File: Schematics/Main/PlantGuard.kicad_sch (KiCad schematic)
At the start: 7 parts, among them M1 Motor_DC, SW1 SW_SP3T, U1 L298N, U2 LM78M05_TO252

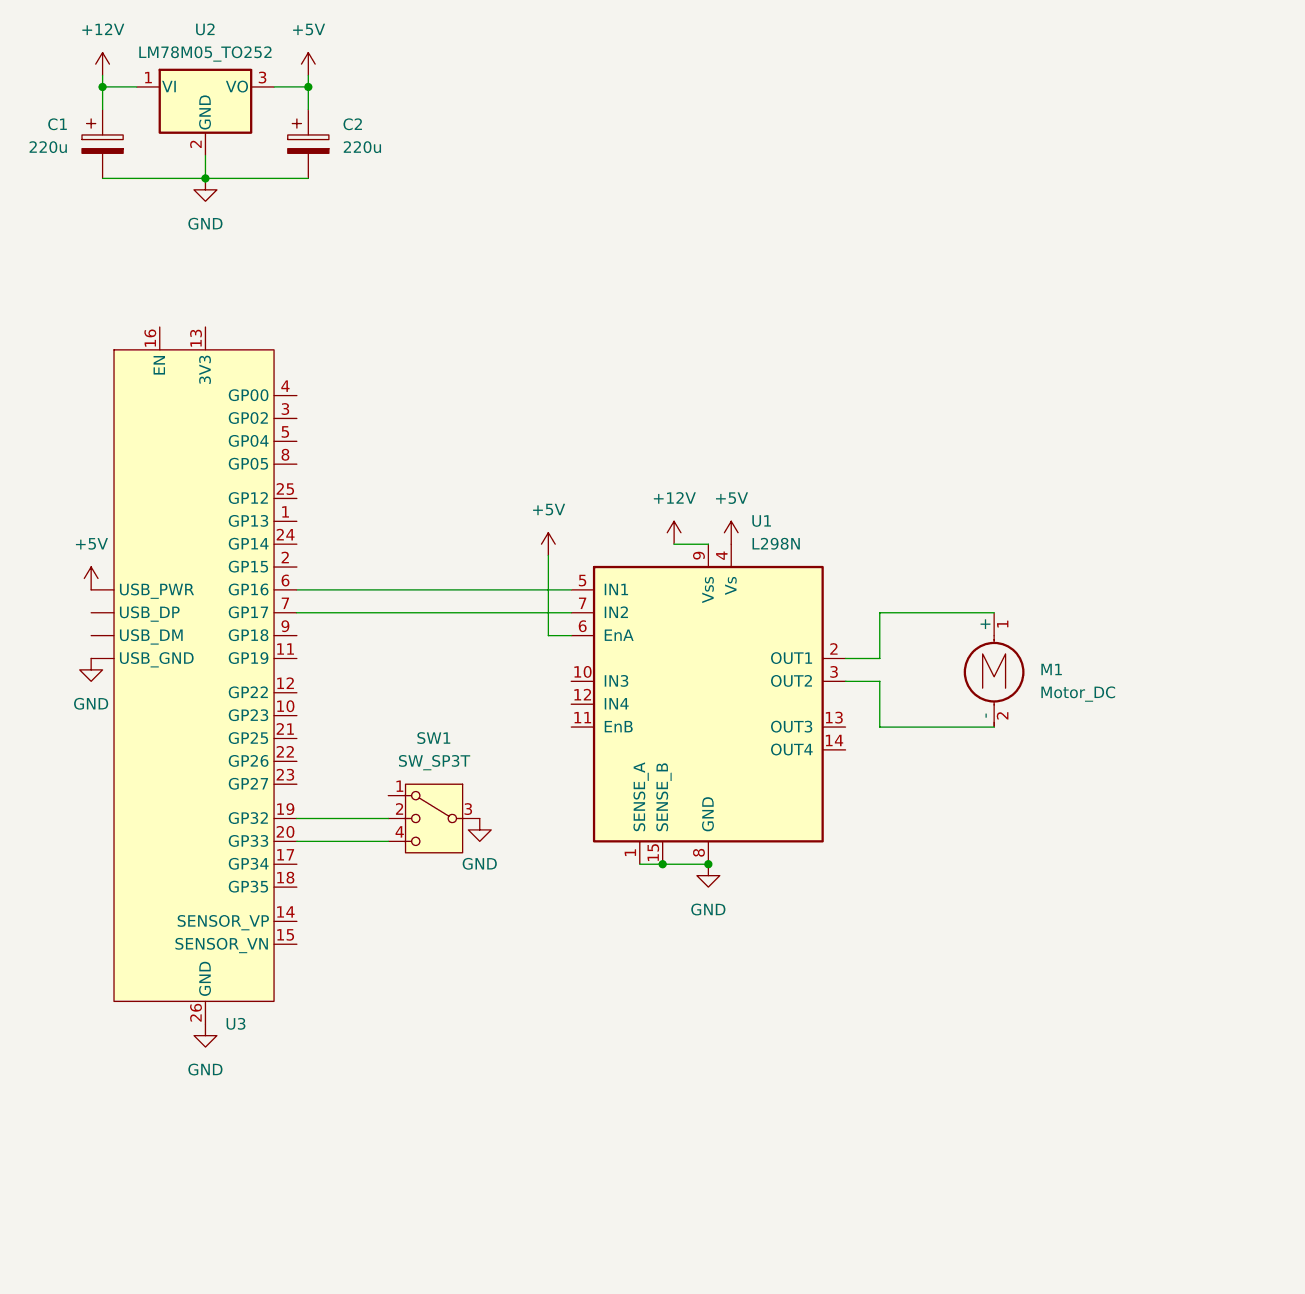
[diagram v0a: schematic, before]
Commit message: Read light intensity from photoresistor
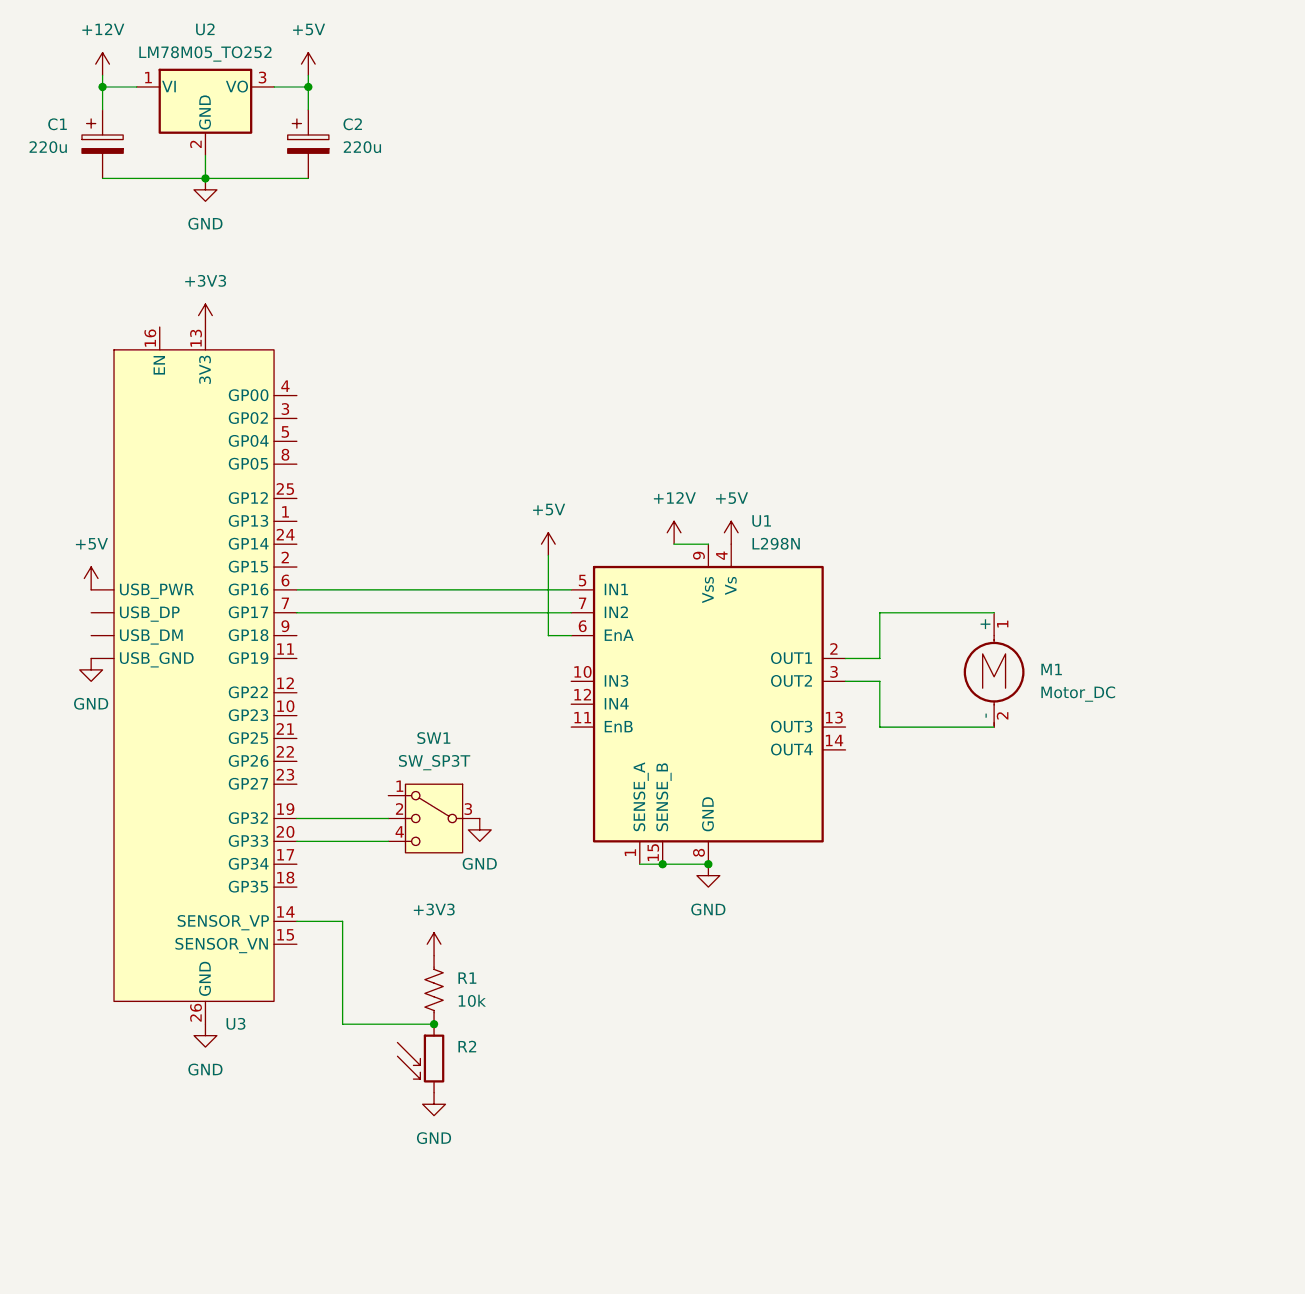
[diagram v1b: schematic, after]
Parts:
- added R1: 10k, symbol Device:R_US
- added R2: (no value), symbol Device:R_Photo
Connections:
- net GND: now also R2.2
- net +3V3: now reaches U3.13 (3V3)
- net +3V3: now also R1.1
- net at U3.14 (SENSOR_VP): now also R1.2, R2.1

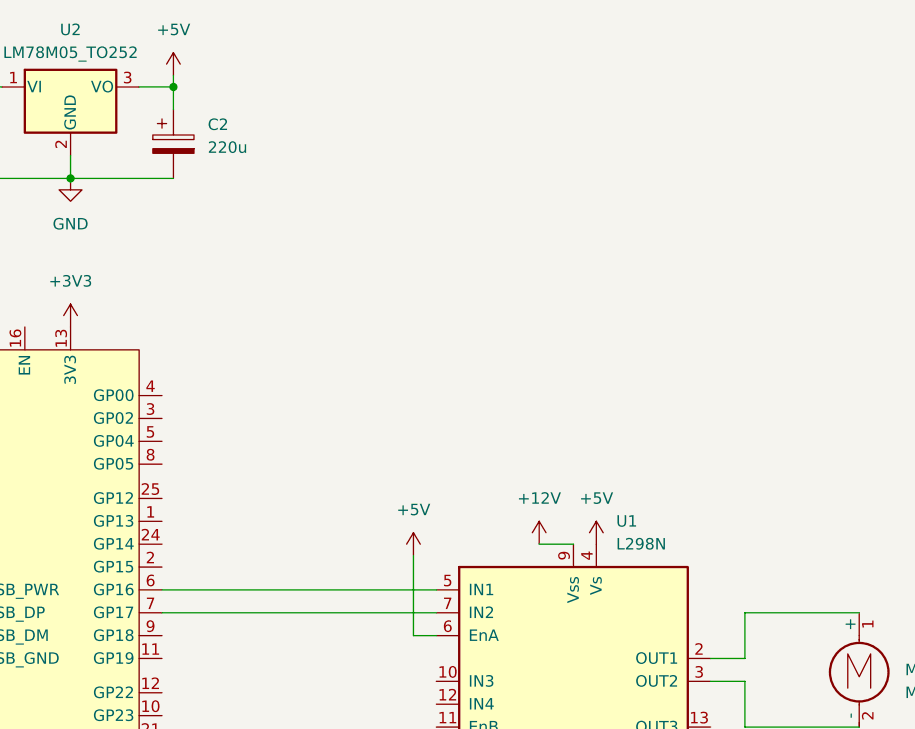
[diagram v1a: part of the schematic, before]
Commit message: Connect the accelerometer
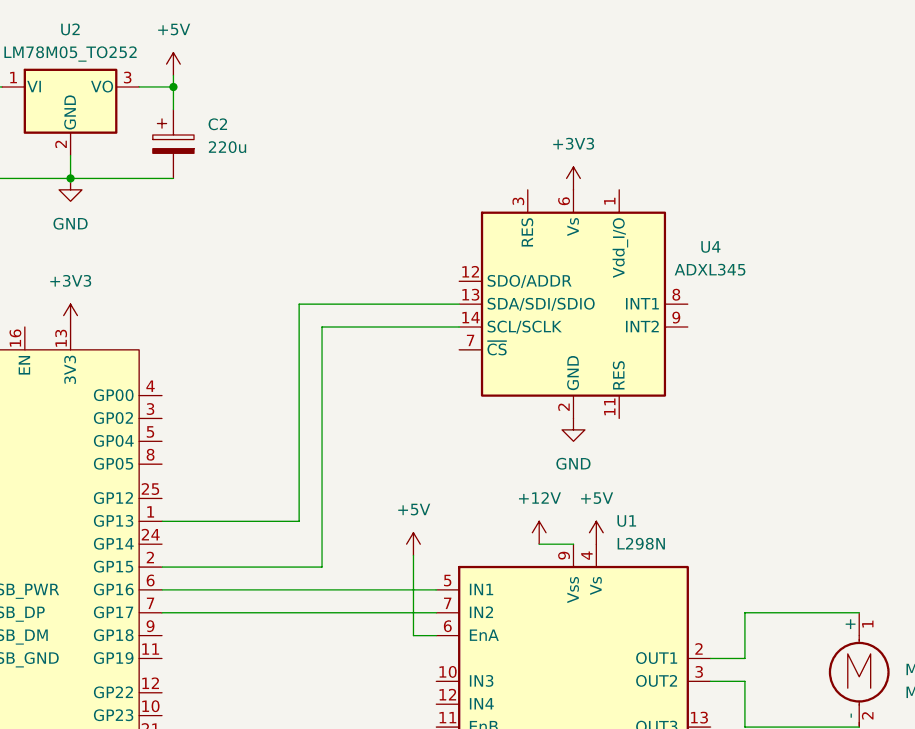
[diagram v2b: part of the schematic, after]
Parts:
- added U4: ADXL345, Package_LGA:LGA-14_3x5mm_P0.8mm_LayoutBorder1x6y, symbol Sensor_Motion:ADXL343
- R2: value (none) -> ~
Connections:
- net +3V3: now also U4.6 (Vs)
- net GND: now also U4.2 (GND), U4.4 (GND), U4.5 (GND)
- net at U3.1 (GP13): now also U4.13 (SDA/SDI/SDIO)
- net at U3.2 (GP15): now also U4.14 (SCL/SCLK)

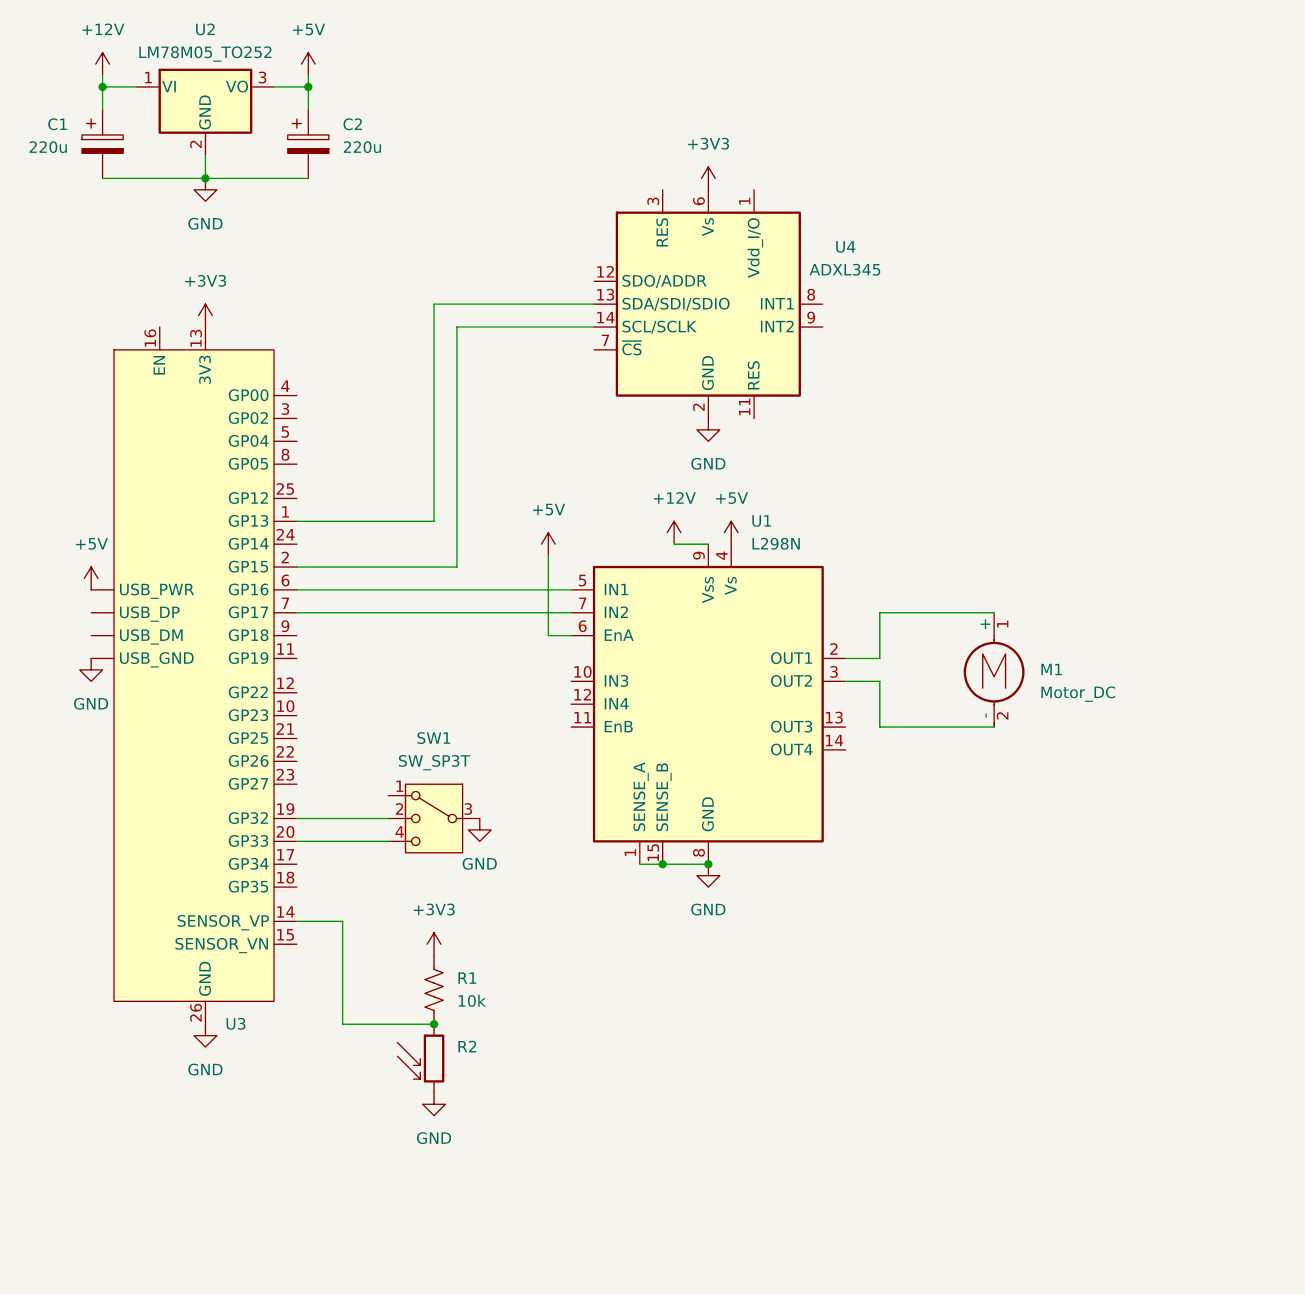
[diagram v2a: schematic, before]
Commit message: Connect ground moisture sensor
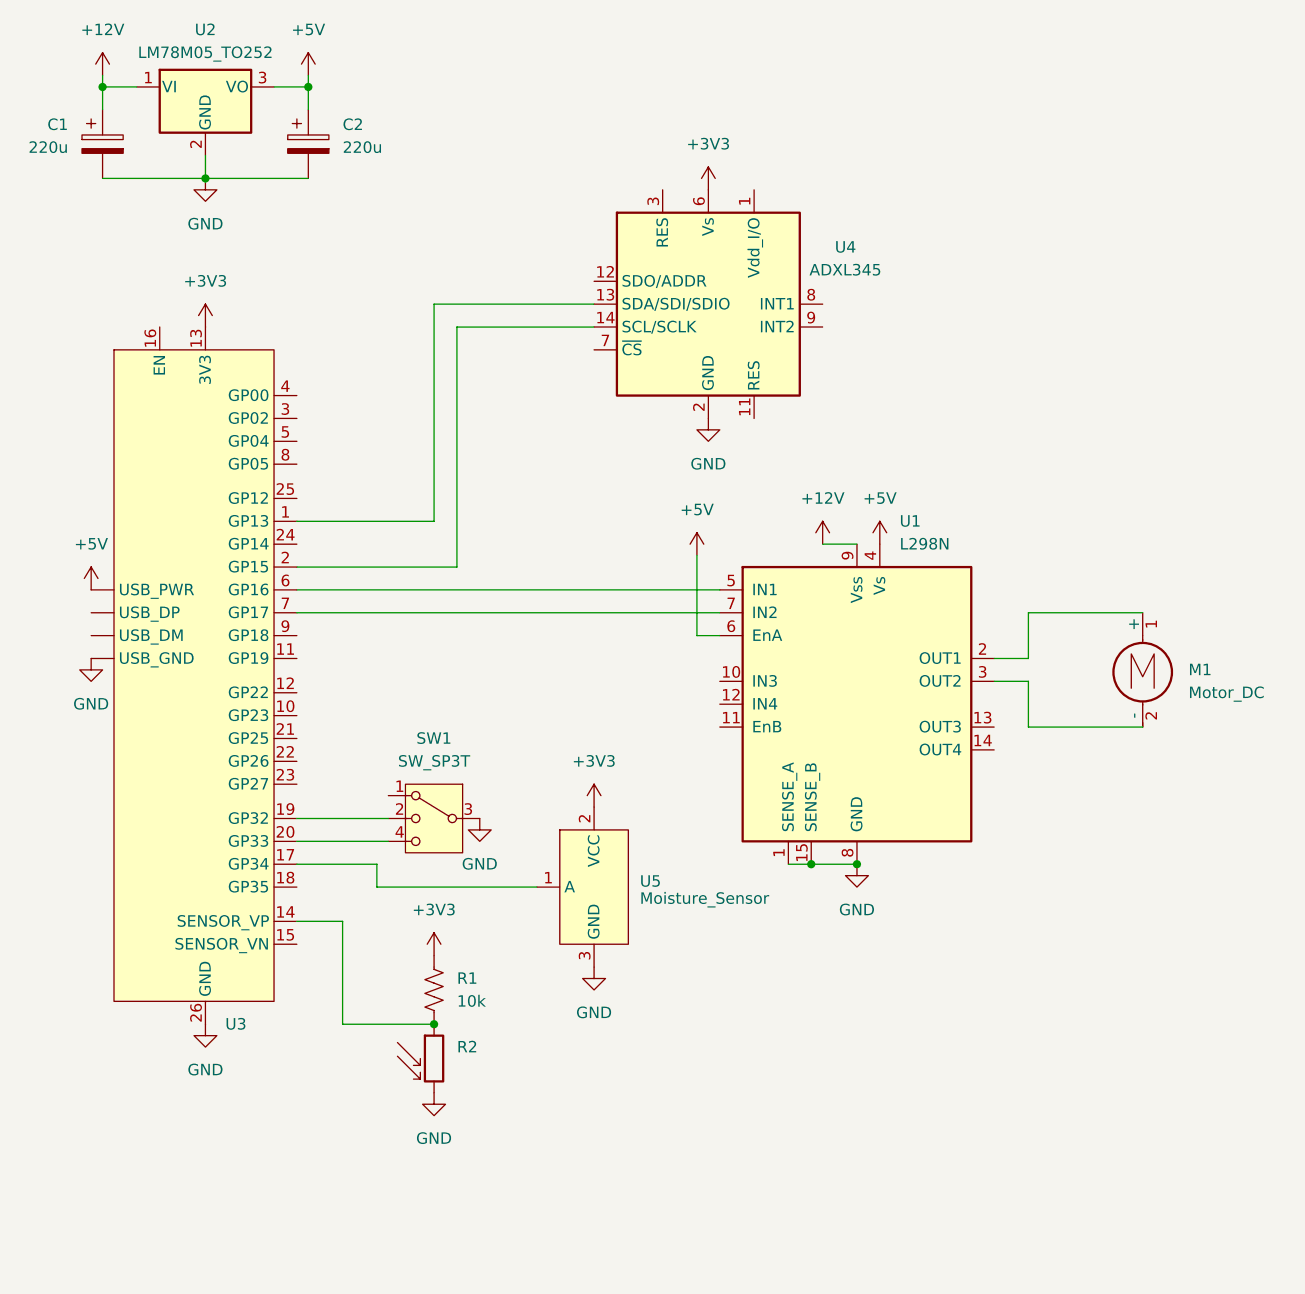
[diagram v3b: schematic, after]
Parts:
- added U5: Moisture_Sensor, symbol ESP32:DFRobot_Moisture_Sensor
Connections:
- net +3V3: now also U5.2 (VCC)
- net GND: now also U5.3 (GND)
- net at U3.17 (GP34): now also U5.1 (A)
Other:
- moved on the sheet: M1, U1

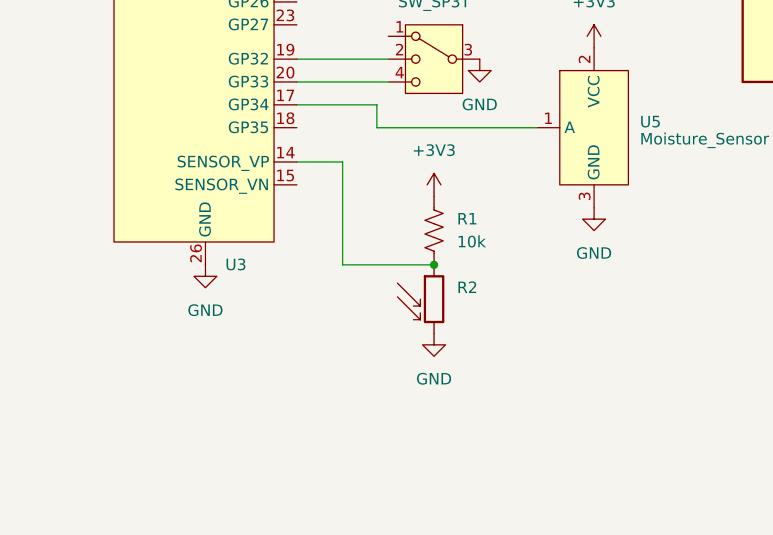
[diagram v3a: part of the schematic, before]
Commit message: Connect the thermistor
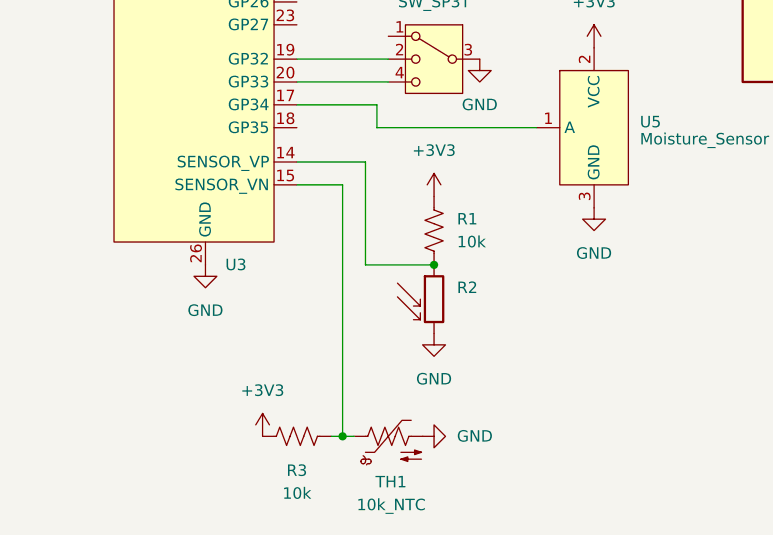
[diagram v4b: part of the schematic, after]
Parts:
- added R3: 10k, symbol Device:R_US
- added TH1: 10k_NTC, symbol Device:Thermistor_NTC_US
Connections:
- net +3V3: now also R3.1
- net GND: now also TH1.2
- net at U3.15 (SENSOR_VN): now also R3.2, TH1.1
